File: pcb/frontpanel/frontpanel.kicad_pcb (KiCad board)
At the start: 2 copper layers, 175.8 x 64 mm, 19 parts, among them J1 xx, J2 xx, J3 xx, J4 xx, Q1 NPN

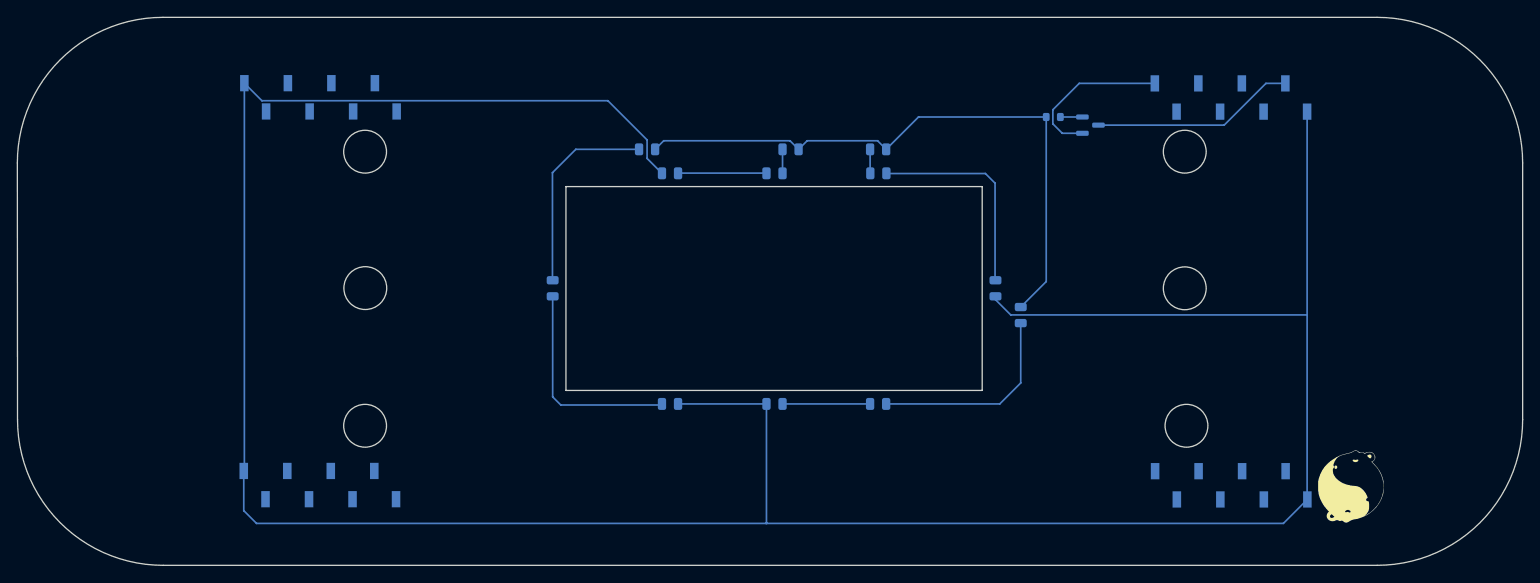
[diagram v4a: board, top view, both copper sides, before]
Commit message: [pcb] use optocoupler in frontpanel
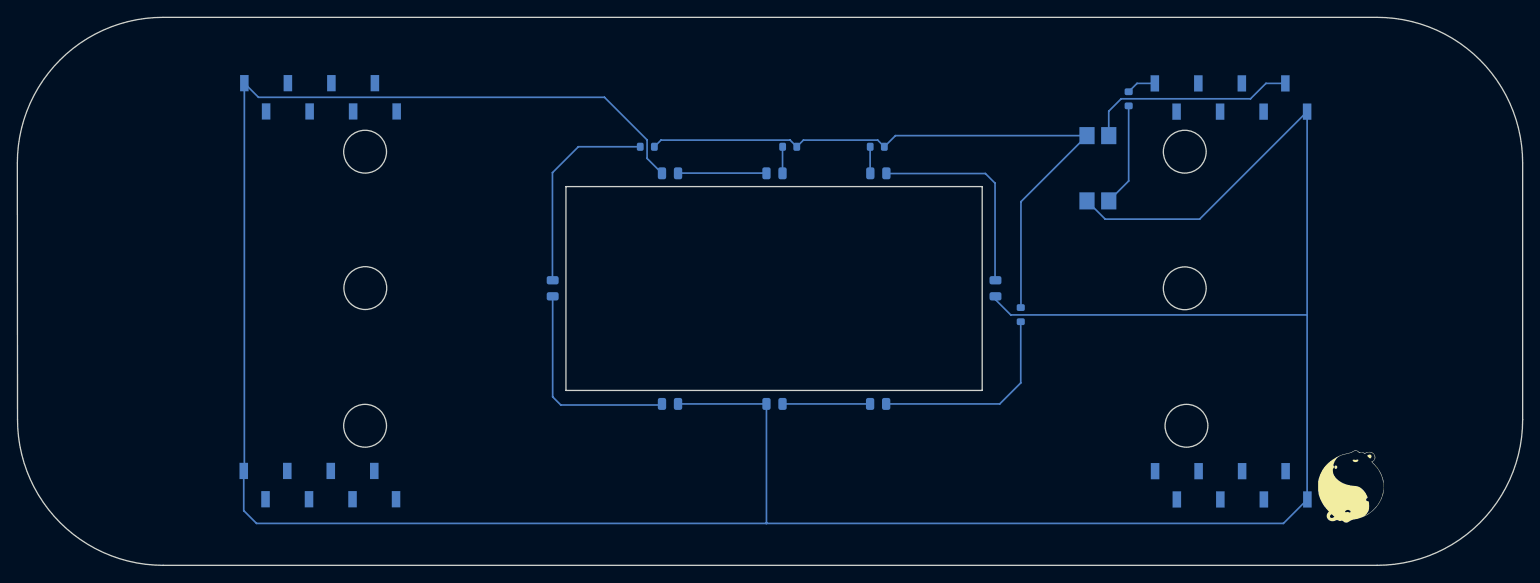
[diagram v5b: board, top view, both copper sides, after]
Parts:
- removed F1, F2, F3, F4: Fuse, Fuse:Fuse_0805_2012Metric
- removed Q1: NPN, Package_TO_SOT_SMD:SOT-23
- added R2: 68, Resistor_SMD:R_0603_1608Metric, B.Cu at (174.0, 109.8)
- added R3: 68, Resistor_SMD:R_0603_1608Metric, B.Cu at (147.1, 90.2)
- added R4: 68, Resistor_SMD:R_0603_1608Metric, B.Cu at (157.3, 90.2)
- added R5: 220, Resistor_SMD:R_0603_1608Metric, B.Cu at (186.6, 84.6)
- added U1: 34.81-7048, Package_DIP:SMDIP-4_W7.62mm, B.Cu at (183.0, 92.7)
- R1: value 330 -> 68
- moved R1 47.5 mm to (130.4, 90.2)
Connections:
- R1 pad 1: Net-(F1-Pad1) -> Net-(D1-A)
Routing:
- net Net-(R1-Pad2): track 2.57 -> 75.5 mm
- net Net-(F1-Pad1): track 72.3 -> 0.00 mm
- net GND: track 337.4 -> 369.2 mm
- net GPIO11: track 18.7 -> 3.46 mm
- net Net-(R5-Pad1): track 0.00 -> 12.1 mm
- net +5V: track 23.8 -> 24.8 mm

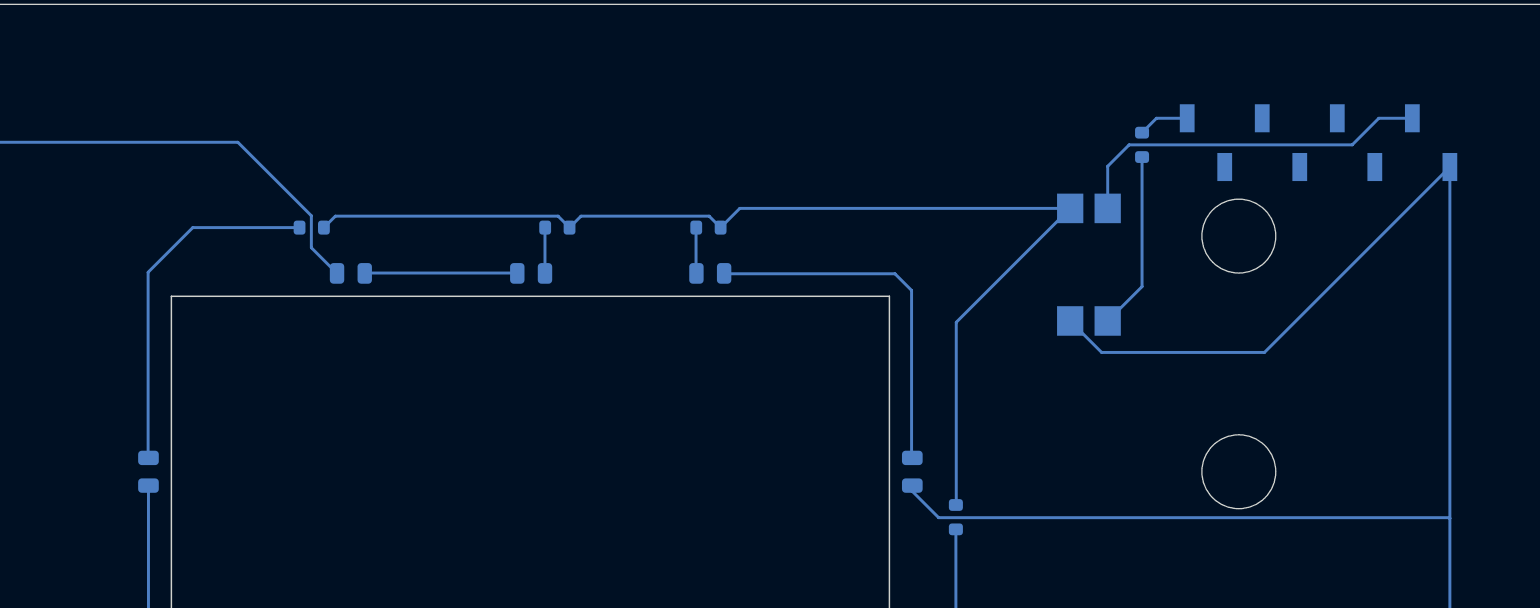
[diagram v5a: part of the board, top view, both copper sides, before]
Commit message: [pcb] mono audio, combined sdcard footprint
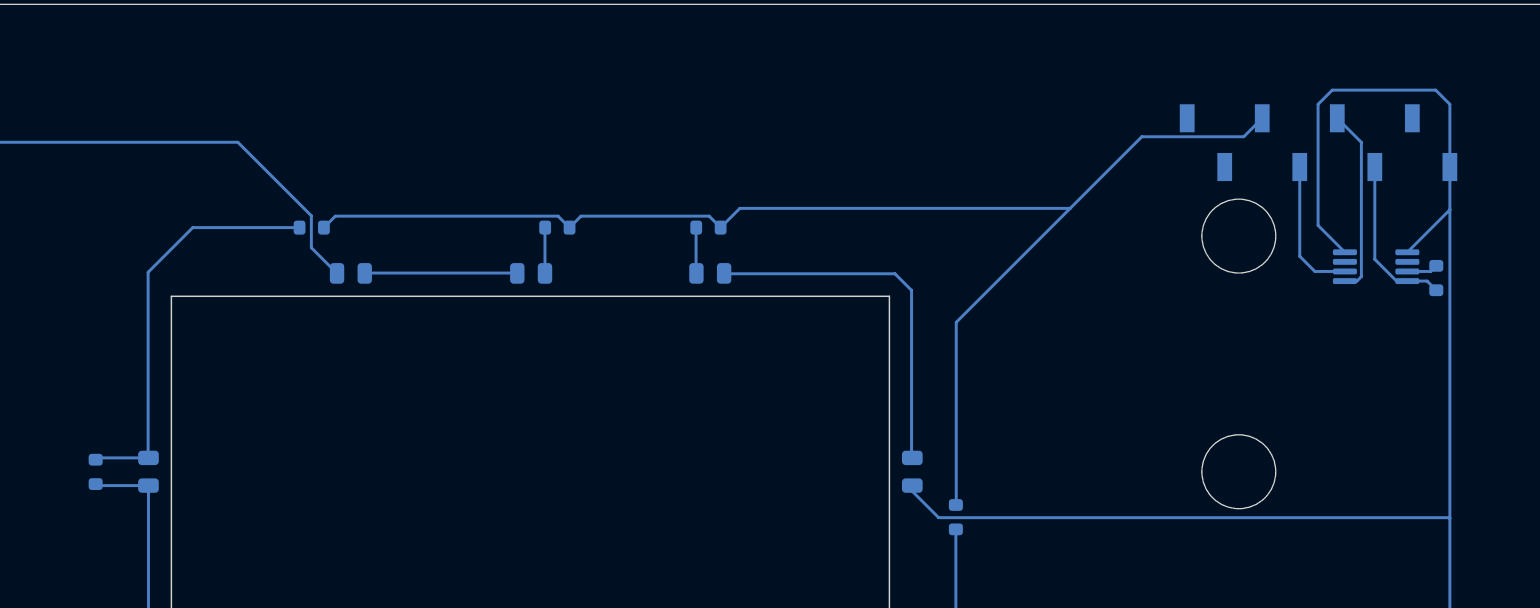
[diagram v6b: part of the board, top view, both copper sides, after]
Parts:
- removed U1: 34.81-7048, Package_DIP:SMDIP-4_W7.62mm
- added R6: 220, Resistor_SMD:R_0603_1608Metric, B.Cu at (206.5, 93.6)
- added U2: MCP9808_MSOP, Package_SO:MSOP-8_3x3mm_P0.65mm, B.Cu at (202.5, 92.9)
- R5: value 220 -> 10K
- moved R5 74.2 mm to (115.8, 106.8)
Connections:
- J1 pad 6: unconnected-(J1-Pin_6-Pad6) -> 5V control
- R1 pad 2: Net-(R1-Pad2) -> 5V control
- R2 pad 2: Net-(R1-Pad2) -> 5V control
- R3 pad 2: Net-(R1-Pad2) -> 5V control
- R4 pad 2: Net-(R1-Pad2) -> 5V control
- R5 pad 1: Net-(R5-Pad1) -> Net-(D1-K)
- R5 pad 2: GPIO11 -> Net-(D1-A)
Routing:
- net 5V control: track 0.00 -> 91.1 mm
- net Net-(R1-Pad2): track 75.5 -> 0.00 mm
- net +5V: track 24.8 -> 0.00 mm
- net SDA: track 0.00 -> 12.6 mm
- net Net-(R5-Pad1): track 12.1 -> 0.00 mm
- net +3.3V: track 0.00 -> 11.3 mm
- net SCL: track 0.00 -> 9.53 mm
- net Net-(D1-A): track 24.1 -> 27.7 mm
- net Net-(D1-K): track 24.9 -> 28.6 mm
- net GPIO11: track 3.46 -> 0.00 mm
- net GND: track 369.2 -> 366.2 mm
- net Net-(U2-A0): track 0.00 -> 2.11 mm
